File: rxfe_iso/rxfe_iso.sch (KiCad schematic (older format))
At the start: 14 parts, among them P1 CONN_02X08, P2 CONN_01X02, P3 CONN_02X08, U1 ADUM6400ARWZ, U2 ADUM7440

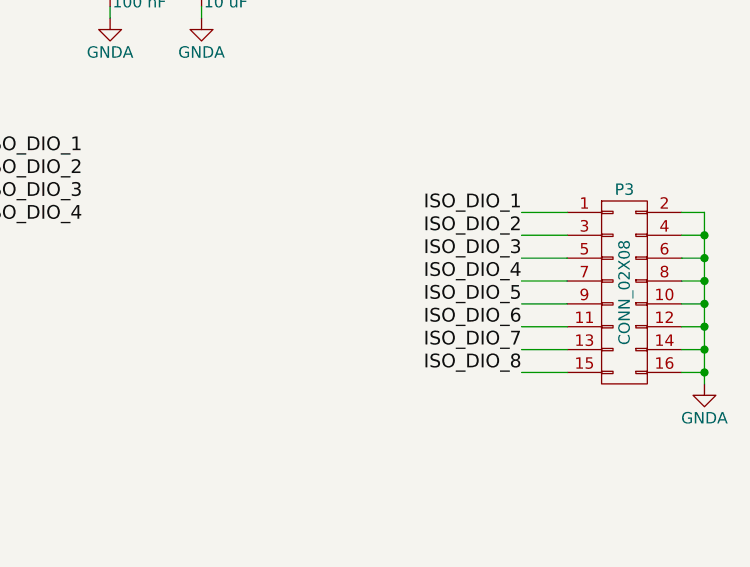
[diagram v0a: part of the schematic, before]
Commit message: added rf-front end module for mcmurdo USRP upgrade
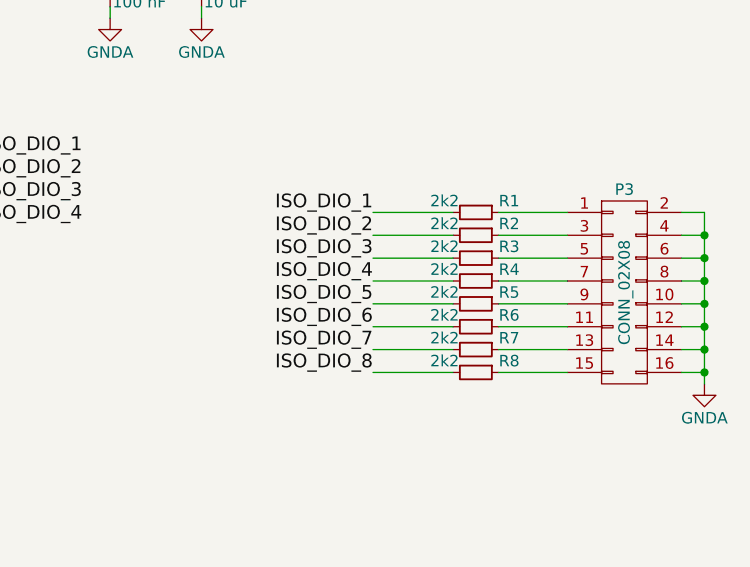
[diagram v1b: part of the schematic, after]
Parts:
- added R1, R2, R3, R4, R5, R6, R7, R8: 2k2, Resistors_SMD:R_0603, symbol R_Small
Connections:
- net ISO_DIO_1: now also R1.2; no longer P3.1 (P1)
- net ISO_DIO_2: now also R2.2; no longer P3.3 (P3)
- net ISO_DIO_3: now also R3.2; no longer P3.5 (P5)
- net ISO_DIO_4: now also R4.2; no longer P3.7 (P7)
- net ISO_DIO_5: now also R5.2; no longer P3.9 (P9)
- net ISO_DIO_6: now also R6.2; no longer P3.11 (P11)
- net ISO_DIO_7: now also R7.2; no longer P3.13 (P13)
- net ISO_DIO_8: now also R8.2; no longer P3.15 (P15)
- new net: P3.1 (P1), R1.1
- new net: P3.11 (P11), R6.1
- new net: P3.13 (P13), R7.1
- new net: P3.15 (P15), R8.1
- new net: P3.3 (P3), R2.1
- new net: P3.5 (P5), R3.1
- new net: P3.7 (P7), R4.1
- new net: P3.9 (P9), R5.1
